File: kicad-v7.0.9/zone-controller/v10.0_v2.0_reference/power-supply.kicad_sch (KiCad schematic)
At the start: 63 parts, among them J13 EBBA-02-C-SS-BU, J14 EBBA-02-C-SS-BU, Q15 AOB1608L, Q17 AOB1608L, Q18 PMV213SN,215, Q19 PMV213SN,215, Q20 AOB1608L, Q21 AOB1608L, Q22 PMV213SN,215, Q23 PMV213SN,215, U27 LM5069, U30 LM5069, U4 TPS26600

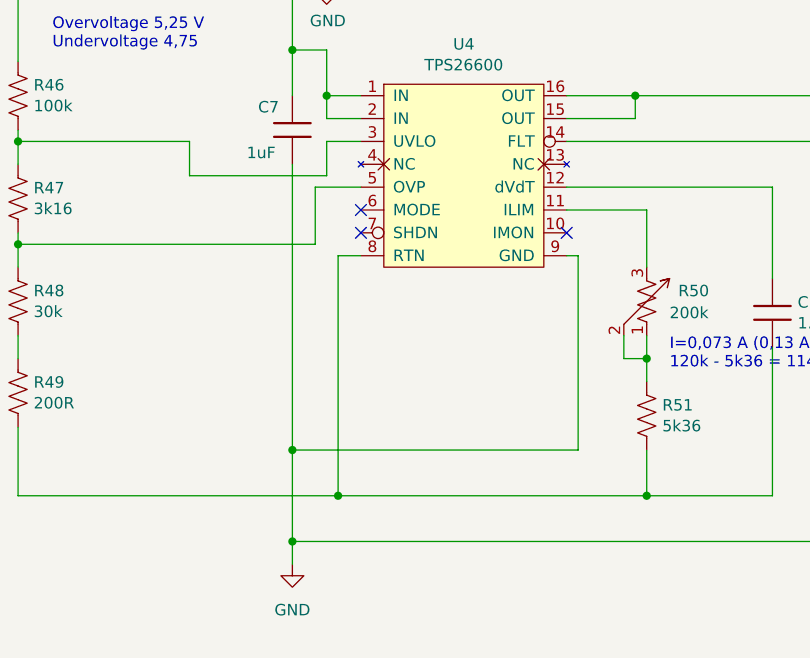
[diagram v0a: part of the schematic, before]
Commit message: Change info and size page in PCB. Small changes in library.
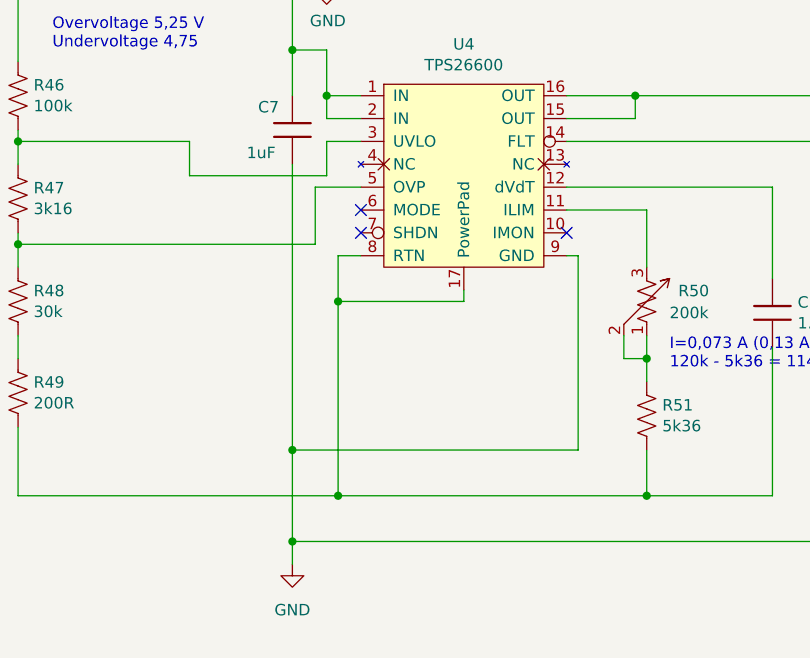
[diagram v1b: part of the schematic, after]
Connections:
- net at C10.2, R49.2, R51.1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: now also U4.17 (PowerPad)
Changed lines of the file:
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@@
   (junction (at 280.67 102.87) (diameter 0) (color 0 0 0 0)
   )
+  (junction (at 285.75 86.36) (diameter 0) (color 0 0 0 0)
+  )
   (junction (at 146.05 208.28) (diameter 0) (color 0 0 0 0)
   )
@@
     (stroke (width 0) (type default))
   )
-  (wire (pts (xy 285.75 81.28) (xy 285.75 107.95))
+  (wire (pts (xy 285.75 81.28) (xy 285.75 86.36))
     (stroke (width 0) (type default))
   )
@@
     (stroke (width 0) (type default))
   )
+  (wire (pts (xy 285.75 86.36) (xy 285.75 107.95))
+    (stroke (width 0) (type default))
+  )
   (wire (pts (xy 92.71 246.38) (xy 106.68 246.38))
     (stroke (width 0) (type default))
@@
     (stroke (width 0) (type default))
   )
+  (wire (pts (xy 299.72 85.09) (xy 299.72 86.36))
+    (stroke (width 0) (type default))
+  )
   (wire (pts (xy 69.85 92.71) (xy 81.28 92.71))
     (stroke (width 0) (type default))
@@
     (stroke (width 0) (type default))
   )
+  (wire (pts (xy 285.75 86.36) (xy 299.72 86.36))
+    (stroke (width 0) (type default))
+  )
   (wire (pts (xy 114.3 92.71) (xy 123.19 92.71))
     (stroke (width 0) (type default))
@@
     (pin "5")
     (pin "9")
-    (pin "8")
+    (pin "17")
     (pin "7")
     (pin "6")

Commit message: Zone controller. Change library. Small changes in schematic a PCB.
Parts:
- C10, C11, C54, C55, C56, C58, C63, C64, C65, C69, C7: symbol passive_component_rl:capacitor -> capacitor_smd_rl:c_1206
- D17, D45, D54: symbol diode_rl:LED -> led_tht_rl:LL-503VC1E-4C
- D39, D48: symbol diode_rl:bidir_transil -> transil_diode_smd_rl:SMBJ24CA-TR
- D40, D41, D49, D51: symbol diode_rl:rectifier_diode -> diode_smd_rl:BAV20WS-DC
- D43, D53: symbol diode_rl:zener_diode -> zener_diode_smd_rl:TZMB27-GS08
- D50: symbol diode_rl:bidir_transil -> transil_diode_smd_rl:SMCJ5.0CA-13-F
- J13, J14: symbol connector_rl:1x2_screw_term_block -> terminal_block_tht_rl:EBBA-02-C-SS-BU
- Q15, Q17, Q20, Q21: symbol unipolar_transistor_rl:n_mosfet_gsd -> unipolar_transistor_smd_rl:AOB1608L
- Q18, Q19, Q22, Q23: symbol unipolar_transistor_rl:n_mosfet_gsd -> unipolar_transistor_smd_rl:PMV213SN,215
- R102, R46, R47, R48, R49, R51, R52, R70, R71, R73, R74, R75, R76, R78, R81, R82, R83, R87, R88, R89, R90, R91, R92, R93, R98, R99: symbol passive_component_rl:resistor_us -> resistor_smd_rl:r_1206_us
- R50: footprint trimmer_tht_rl:trimmer_t93yb -> trimmer_tht_rl:T93YB; symbol passive_component_rl:resistor_variable_us -> trimmer_tht_rl:T93YB; Manufacturer (none) -> Vishay
- U4: Manufacturer (none) -> Texas Instruments
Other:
- moved on the sheet: D40, D41, D49, D50, D51
